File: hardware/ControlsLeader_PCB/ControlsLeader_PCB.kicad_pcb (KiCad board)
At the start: 2 copper layers, 72.5 x 61.5 mm, 3 parts, among them J1 CarCANConnector, J2 PeripheralCAN, U1 LeaderSOM

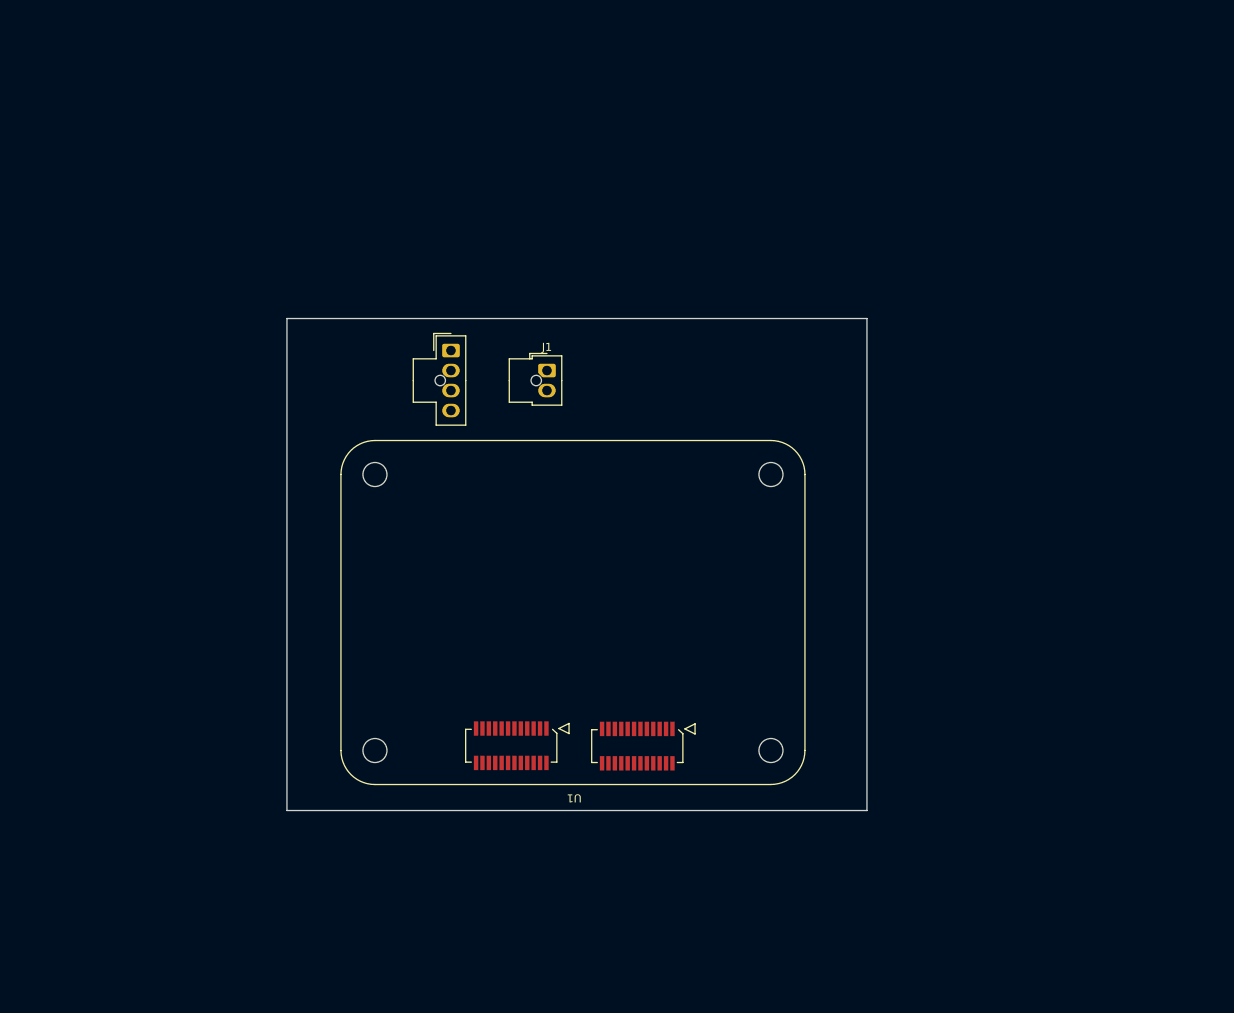
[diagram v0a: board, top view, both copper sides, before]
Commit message: Schematic Ready for Review - Just need FET footprints to be confirmed
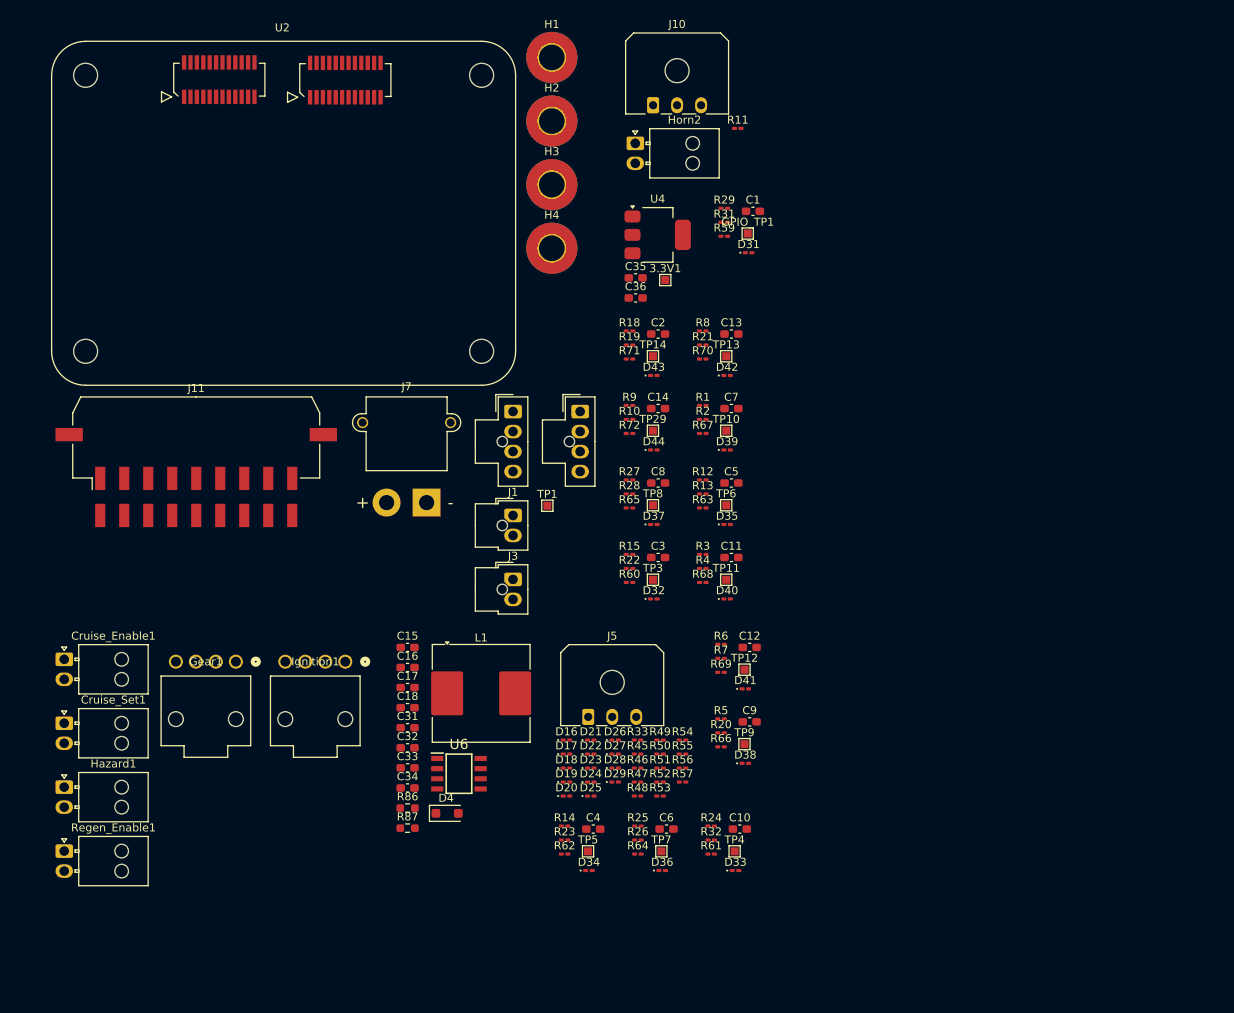
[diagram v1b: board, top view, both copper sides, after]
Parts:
- removed U1: LeaderSOM, UTSVT_Special:LeaderSOM
- added 3.3V1: TestPoint, TestPoint:TestPoint_Pad_1.0x1.0mm, F.Cu at (157.8, 68.2)
- added C1: 5uF, Capacitor_SMD:C_0603_1608Metric_Pad1.08x0.95mm_HandSolder, F.Cu at (168.7, 59.6)
- added C10: 5uF, Capacitor_SMD:C_0603_1608Metric_Pad1.08x0.95mm_HandSolder, F.Cu at (167.1, 136.8)
- added C11: 5uF, Capacitor_SMD:C_0603_1608Metric_Pad1.08x0.95mm_HandSolder, F.Cu at (166.1, 102.9)
- added C12: 5uF, Capacitor_SMD:C_0603_1608Metric_Pad1.08x0.95mm_HandSolder, F.Cu at (168.3, 114.1)
- added C13: 5uF, Capacitor_SMD:C_0603_1608Metric_Pad1.08x0.95mm_HandSolder, F.Cu at (166.1, 74.9)
- added C14: 5uF, Capacitor_SMD:C_0603_1608Metric_Pad1.08x0.95mm_HandSolder, F.Cu at (156.9, 84.2)
- added C15: 10uF, Capacitor_SMD:C_0603_1608Metric_Pad1.08x0.95mm_HandSolder, F.Cu at (125.6, 114.1)
- added C16: 1uF, Capacitor_SMD:C_0603_1608Metric_Pad1.08x0.95mm_HandSolder, F.Cu at (125.6, 116.6)
- added C17: 10nF, Capacitor_SMD:C_0603_1608Metric_Pad1.08x0.95mm_HandSolder, F.Cu at (125.6, 119.1)
- added C18: 3.3nF, Capacitor_SMD:C_0603_1608Metric_Pad1.08x0.95mm_HandSolder, F.Cu at (125.6, 121.6)
- added C2: 5uF, Capacitor_SMD:C_0603_1608Metric_Pad1.08x0.95mm_HandSolder, F.Cu at (156.9, 74.9)
- added C3: 5uF, Capacitor_SMD:C_0603_1608Metric_Pad1.08x0.95mm_HandSolder, F.Cu at (156.9, 102.9)
- added C31: 0.1uF, Capacitor_SMD:C_0603_1608Metric_Pad1.08x0.95mm_HandSolder, F.Cu at (125.6, 124.2)
- added C32: 10uF, Capacitor_SMD:C_0603_1608Metric_Pad1.08x0.95mm_HandSolder, F.Cu at (125.6, 126.7)
- added C33: 10uF, Capacitor_SMD:C_0603_1608Metric_Pad1.08x0.95mm_HandSolder, F.Cu at (125.6, 129.2)
- added C34: 10uF, Capacitor_SMD:C_0603_1608Metric_Pad1.08x0.95mm_HandSolder, F.Cu at (125.6, 131.7)
- added C35: 10uF, Capacitor_SMD:C_0603_1608Metric_Pad1.08x0.95mm_HandSolder, F.Cu at (154.1, 67.9)
- added C36: 10uF, Capacitor_SMD:C_0603_1608Metric_Pad1.08x0.95mm_HandSolder, F.Cu at (154.1, 70.4)
- added C4: 5uF, Capacitor_SMD:C_0603_1608Metric_Pad1.08x0.95mm_HandSolder, F.Cu at (148.8, 136.8)
- added C5: 5uF, Capacitor_SMD:C_0603_1608Metric_Pad1.08x0.95mm_HandSolder, F.Cu at (166.1, 93.6)
- added C6: 5uF, Capacitor_SMD:C_0603_1608Metric_Pad1.08x0.95mm_HandSolder, F.Cu at (157.9, 136.8)
- added C7: 5uF, Capacitor_SMD:C_0603_1608Metric_Pad1.08x0.95mm_HandSolder, F.Cu at (166.1, 84.2)
- added C8: 5uF, Capacitor_SMD:C_0603_1608Metric_Pad1.08x0.95mm_HandSolder, F.Cu at (156.9, 93.6)
- added C9: 5uF, Capacitor_SMD:C_0603_1608Metric_Pad1.08x0.95mm_HandSolder, F.Cu at (168.3, 123.4)
- added Cruise_Enable1: SW_Push, Connector_Molex:Molex_Nano-Fit_105313-xx02_1x02_P2.50mm_Horizontal, F.Cu at (82.7, 115.6)
- added Cruise_Set1: SW_Push, Connector_Molex:Molex_Nano-Fit_105313-xx02_1x02_P2.50mm_Horizontal, F.Cu at (82.7, 123.6)
- added D16: 0603_SMD, LED_SMD:LED_0201_0603Metric_Pad0.64x0.40mm_HandSolder, F.Cu at (145.4, 125.7)
- added D17: 0603_SMD, LED_SMD:LED_0201_0603Metric_Pad0.64x0.40mm_HandSolder, F.Cu at (145.4, 127.4)
- added D18: 0603_SMD, LED_SMD:LED_0201_0603Metric_Pad0.64x0.40mm_HandSolder, F.Cu at (145.4, 129.2)
- added D19: 0603_SMD, LED_SMD:LED_0201_0603Metric_Pad0.64x0.40mm_HandSolder, F.Cu at (145.4, 130.9)
- added D20: 0603_SMD, LED_SMD:LED_0201_0603Metric_Pad0.64x0.40mm_HandSolder, F.Cu at (145.4, 132.7)
- added D21: 0603_SMD, LED_SMD:LED_0201_0603Metric_Pad0.64x0.40mm_HandSolder, F.Cu at (148.5, 125.7)
- added D22: 0603_SMD, LED_SMD:LED_0201_0603Metric_Pad0.64x0.40mm_HandSolder, F.Cu at (148.5, 127.4)
- added D23: 0603_SMD, LED_SMD:LED_0201_0603Metric_Pad0.64x0.40mm_HandSolder, F.Cu at (148.5, 129.2)
- added D24: 0603_SMD, LED_SMD:LED_0201_0603Metric_Pad0.64x0.40mm_HandSolder, F.Cu at (148.5, 130.9)
- added D25: 0603_SMD, LED_SMD:LED_0201_0603Metric_Pad0.64x0.40mm_HandSolder, F.Cu at (148.5, 132.7)
- added D26: 0603_SMD, LED_SMD:LED_0201_0603Metric_Pad0.64x0.40mm_HandSolder, F.Cu at (151.5, 125.7)
- added D27: 0603_SMD, LED_SMD:LED_0201_0603Metric_Pad0.64x0.40mm_HandSolder, F.Cu at (151.5, 127.4)
- added D28: 0603_SMD, LED_SMD:LED_0201_0603Metric_Pad0.64x0.40mm_HandSolder, F.Cu at (151.5, 129.2)
- added D29: 0603_SMD, LED_SMD:LED_0201_0603Metric_Pad0.64x0.40mm_HandSolder, F.Cu at (151.5, 130.9)
- added D31: GPIO_Status_Blue, LED_SMD:LED_0201_0603Metric_Pad0.64x0.40mm_HandSolder, F.Cu at (168.2, 64.8)
- added D32: GPIO_Status_Blue, LED_SMD:LED_0201_0603Metric_Pad0.64x0.40mm_HandSolder, F.Cu at (156.4, 108.0)
- added D33: GPIO_Status_Blue, LED_SMD:LED_0201_0603Metric_Pad0.64x0.40mm_HandSolder, F.Cu at (166.6, 142.0)
- added D34: GPIO_Status_Blue, LED_SMD:LED_0201_0603Metric_Pad0.64x0.40mm_HandSolder, F.Cu at (148.2, 142.0)
- added D35: GPIO_Status_Blue, LED_SMD:LED_0201_0603Metric_Pad0.64x0.40mm_HandSolder, F.Cu at (165.5, 98.7)
- added D36: GPIO_Status_Blue, LED_SMD:LED_0201_0603Metric_Pad0.64x0.40mm_HandSolder, F.Cu at (157.4, 142.0)
- added D37: GPIO_Status_Blue, LED_SMD:LED_0201_0603Metric_Pad0.64x0.40mm_HandSolder, F.Cu at (156.4, 98.7)
- added D38: GPIO_Status_Blue, LED_SMD:LED_0201_0603Metric_Pad0.64x0.40mm_HandSolder, F.Cu at (167.8, 128.6)
- added D39: GPIO_Status_Blue, LED_SMD:LED_0201_0603Metric_Pad0.64x0.40mm_HandSolder, F.Cu at (165.5, 89.4)
- added D4: MBR230S1F, Diode_SMD:D_SOD-123F, F.Cu at (130.5, 134.8)
- added D40: GPIO_Status_Blue, LED_SMD:LED_0201_0603Metric_Pad0.64x0.40mm_HandSolder, F.Cu at (165.5, 108.0)
- added D41: GPIO_Status_Blue, LED_SMD:LED_0201_0603Metric_Pad0.64x0.40mm_HandSolder, F.Cu at (167.8, 119.3)
- added D42: GPIO_Status_Blue, LED_SMD:LED_0201_0603Metric_Pad0.64x0.40mm_HandSolder, F.Cu at (165.5, 80.1)
- added D43: GPIO_Status_Blue, LED_SMD:LED_0201_0603Metric_Pad0.64x0.40mm_HandSolder, F.Cu at (156.4, 80.1)
- added D44: GPIO_Status_Blue, LED_SMD:LED_0201_0603Metric_Pad0.64x0.40mm_HandSolder, F.Cu at (156.4, 89.4)
- added GPIO_TP1: TestPoint, TestPoint:TestPoint_Pad_1.0x1.0mm, F.Cu at (168.1, 62.4)
- added Gear1: SW_SP3T, nanofits_1x04:CONN_SD-105313-100_04_MOL, F.Cu at (104.1, 115.9)
- added H1: M.3, MountingHole:MountingHole_3.2mm_M3_Pad_TopBottom, F.Cu at (143.6, 40.4)
- added H2: M.3, MountingHole:MountingHole_3.2mm_M3_Pad_TopBottom, F.Cu at (143.6, 48.3)
- added H3: M.3, MountingHole:MountingHole_3.2mm_M3_Pad_TopBottom, F.Cu at (143.6, 56.3)
- added H4: M.3, MountingHole:MountingHole_3.2mm_M3_Pad_TopBottom, F.Cu at (143.6, 64.2)
- added Hazard1: SW_Push, Connector_Molex:Molex_Nano-Fit_105313-xx02_1x02_P2.50mm_Horizontal, F.Cu at (82.7, 131.6)
- added Horn2: SW_Push, Connector_Molex:Molex_Nano-Fit_105313-xx02_1x02_P2.50mm_Horizontal, F.Cu at (154.0, 51.1)
- added Ignition1: SW_SP3T, nanofits_1x04:CONN_SD-105313-100_04_MOL, F.Cu at (117.8, 115.9)
- added J10: Indicator_Switch, Connector_Molex:Molex_Micro-Fit_3.0_43650-0300_1x03_P3.00mm_Horizontal, F.Cu at (156.3, 46.3)
- added J11: Nanofit_2Rows-19Pins, Connector_Molex:Molex_Micro-Fit_3.0_43045-1810_2x09-1MP_P3.00mm_Horizontal, F.Cu at (99.2, 95.3)
- added J3: CarCANConnector_In, UTSVT_Connectors:Molex_Nano-Fit_105309-xx02_1x02_P2.50mm_Vertical, F.Cu at (138.8, 105.6)
- added J4: PeripheralCAN_in, UTSVT_Connectors:Molex_Nano-Fit_105309-xx04_1x04_P2.50mm_Vertical, F.Cu at (146.9, 87.7)
- added J5: BPS_Fault_LED, Connector_Molex:Molex_Micro-Fit_3.0_43650-0300_1x03_P3.00mm_Horizontal, F.Cu at (148.2, 122.8)
- added J7: Dash_LSOM_PWR, UTSVT_Connectors:AMASS_XT30PW-M_1x02_P2.50mm_Horizontal, F.Cu at (128.0, 96.0)
- added L1: 100uH, Inductor_SMD:L_Coilcraft_MSS1246-XXX, F.Cu at (134.8, 119.9)
- added R1: 10k, Capacitor_SMD:C_0201_0603Metric_Pad0.64x0.40mm_HandSolder, F.Cu at (162.5, 83.9)
- added R10: 100k, Capacitor_SMD:C_0201_0603Metric_Pad0.64x0.40mm_HandSolder, F.Cu at (153.3, 85.6)
- added R11: 10k, Capacitor_SMD:C_0201_0603Metric_Pad0.64x0.40mm_HandSolder, F.Cu at (166.8, 49.2)
- added R12: 10k, Capacitor_SMD:C_0201_0603Metric_Pad0.64x0.40mm_HandSolder, F.Cu at (162.5, 93.2)
- added R13: 100k, Capacitor_SMD:C_0201_0603Metric_Pad0.64x0.40mm_HandSolder, F.Cu at (162.5, 94.9)
- added R14: 10k, Capacitor_SMD:C_0201_0603Metric_Pad0.64x0.40mm_HandSolder, F.Cu at (145.2, 136.4)
- added R15: 10k, Capacitor_SMD:C_0201_0603Metric_Pad0.64x0.40mm_HandSolder, F.Cu at (153.3, 102.5)
- added R18: 10k, Capacitor_SMD:C_0201_0603Metric_Pad0.64x0.40mm_HandSolder, F.Cu at (153.3, 74.6)
- added R19: 100k, Capacitor_SMD:C_0201_0603Metric_Pad0.64x0.40mm_HandSolder, F.Cu at (153.3, 76.3)
- added R2: 100k, Capacitor_SMD:C_0201_0603Metric_Pad0.64x0.40mm_HandSolder, F.Cu at (162.5, 85.6)
- added R20: 100k, Capacitor_SMD:C_0201_0603Metric_Pad0.64x0.40mm_HandSolder, F.Cu at (164.8, 124.8)
- added R21: 100k, Capacitor_SMD:C_0201_0603Metric_Pad0.64x0.40mm_HandSolder, F.Cu at (162.5, 76.3)
- added R22: 100k, Capacitor_SMD:C_0201_0603Metric_Pad0.64x0.40mm_HandSolder, F.Cu at (153.3, 104.2)
- added R23: 100k, Capacitor_SMD:C_0201_0603Metric_Pad0.64x0.40mm_HandSolder, F.Cu at (145.2, 138.2)
- added R24: 10k, Capacitor_SMD:C_0201_0603Metric_Pad0.64x0.40mm_HandSolder, F.Cu at (163.5, 136.4)
- added R25: 10k, Capacitor_SMD:C_0201_0603Metric_Pad0.64x0.40mm_HandSolder, F.Cu at (154.4, 136.4)
- added R26: 100k, Capacitor_SMD:C_0201_0603Metric_Pad0.64x0.40mm_HandSolder, F.Cu at (154.4, 138.2)
- added R27: 10k, Capacitor_SMD:C_0201_0603Metric_Pad0.64x0.40mm_HandSolder, F.Cu at (153.3, 93.2)
- added R28: 100k, Capacitor_SMD:C_0201_0603Metric_Pad0.64x0.40mm_HandSolder, F.Cu at (153.3, 94.9)
- added R29: 10k, Capacitor_SMD:C_0201_0603Metric_Pad0.64x0.40mm_HandSolder, F.Cu at (165.2, 59.2)
- added R3: 10k, Capacitor_SMD:C_0201_0603Metric_Pad0.64x0.40mm_HandSolder, F.Cu at (162.5, 102.5)
- added R31: 100k, Capacitor_SMD:C_0201_0603Metric_Pad0.64x0.40mm_HandSolder, F.Cu at (165.2, 61.0)
- added R32: 100k, Capacitor_SMD:C_0201_0603Metric_Pad0.64x0.40mm_HandSolder, F.Cu at (163.5, 138.2)
- added R33: 65, Capacitor_SMD:C_0201_0603Metric_Pad0.64x0.40mm_HandSolder, F.Cu at (154.3, 125.7)
- added R4: 100k, Capacitor_SMD:C_0201_0603Metric_Pad0.64x0.40mm_HandSolder, F.Cu at (162.5, 104.2)
- added R45: 65, Capacitor_SMD:C_0201_0603Metric_Pad0.64x0.40mm_HandSolder, F.Cu at (154.3, 127.4)
- added R46: 65, Capacitor_SMD:C_0201_0603Metric_Pad0.64x0.40mm_HandSolder, F.Cu at (154.3, 129.2)
- added R47: 1.1k, Capacitor_SMD:C_0201_0603Metric_Pad0.64x0.40mm_HandSolder, F.Cu at (154.3, 130.9)
- added R48: 20, Capacitor_SMD:C_0201_0603Metric_Pad0.64x0.40mm_HandSolder, F.Cu at (154.3, 132.7)
- added R49: 20, Capacitor_SMD:C_0201_0603Metric_Pad0.64x0.40mm_HandSolder, F.Cu at (157.1, 125.7)
- added R5: 10k, Capacitor_SMD:C_0201_0603Metric_Pad0.64x0.40mm_HandSolder, F.Cu at (164.8, 123.0)
- added R50: 20, Capacitor_SMD:C_0201_0603Metric_Pad0.64x0.40mm_HandSolder, F.Cu at (157.1, 127.4)
- added R51: 20, Capacitor_SMD:C_0201_0603Metric_Pad0.64x0.40mm_HandSolder, F.Cu at (157.1, 129.2)
- added R52: 20, Capacitor_SMD:C_0201_0603Metric_Pad0.64x0.40mm_HandSolder, F.Cu at (157.1, 130.9)
- added R53: 20, Capacitor_SMD:C_0201_0603Metric_Pad0.64x0.40mm_HandSolder, F.Cu at (157.1, 132.7)
- added R54: 20, Capacitor_SMD:C_0201_0603Metric_Pad0.64x0.40mm_HandSolder, F.Cu at (159.9, 125.7)
- added R55: 65, Capacitor_SMD:C_0201_0603Metric_Pad0.64x0.40mm_HandSolder, F.Cu at (159.9, 127.4)
- added R56: 65, Capacitor_SMD:C_0201_0603Metric_Pad0.64x0.40mm_HandSolder, F.Cu at (159.9, 129.2)
- added R57: 65, Capacitor_SMD:C_0201_0603Metric_Pad0.64x0.40mm_HandSolder, F.Cu at (159.9, 130.9)
- added R59: 150, Capacitor_SMD:C_0201_0603Metric_Pad0.64x0.40mm_HandSolder, F.Cu at (165.2, 62.7)
- added R6: 10k, Capacitor_SMD:C_0201_0603Metric_Pad0.64x0.40mm_HandSolder, F.Cu at (164.8, 113.7)
- added R60: 150, Capacitor_SMD:C_0201_0603Metric_Pad0.64x0.40mm_HandSolder, F.Cu at (153.3, 106.0)
- added R61: 150, Capacitor_SMD:C_0201_0603Metric_Pad0.64x0.40mm_HandSolder, F.Cu at (163.5, 139.9)
- added R62: 150, Capacitor_SMD:C_0201_0603Metric_Pad0.64x0.40mm_HandSolder, F.Cu at (145.2, 139.9)
- added R63: 150, Capacitor_SMD:C_0201_0603Metric_Pad0.64x0.40mm_HandSolder, F.Cu at (162.5, 96.7)
- added R64: 150, Capacitor_SMD:C_0201_0603Metric_Pad0.64x0.40mm_HandSolder, F.Cu at (154.4, 139.9)
- added R65: 150, Capacitor_SMD:C_0201_0603Metric_Pad0.64x0.40mm_HandSolder, F.Cu at (153.3, 96.7)
- added R66: 150, Capacitor_SMD:C_0201_0603Metric_Pad0.64x0.40mm_HandSolder, F.Cu at (164.8, 126.5)
- added R67: 150, Capacitor_SMD:C_0201_0603Metric_Pad0.64x0.40mm_HandSolder, F.Cu at (162.5, 87.4)
- added R68: 150, Capacitor_SMD:C_0201_0603Metric_Pad0.64x0.40mm_HandSolder, F.Cu at (162.5, 106.0)
- added R69: 150, Capacitor_SMD:C_0201_0603Metric_Pad0.64x0.40mm_HandSolder, F.Cu at (164.8, 117.2)
- added R7: 100k, Capacitor_SMD:C_0201_0603Metric_Pad0.64x0.40mm_HandSolder, F.Cu at (164.8, 115.5)
- added R70: 150, Capacitor_SMD:C_0201_0603Metric_Pad0.64x0.40mm_HandSolder, F.Cu at (162.5, 78.1)
- added R71: 150, Capacitor_SMD:C_0201_0603Metric_Pad0.64x0.40mm_HandSolder, F.Cu at (153.3, 78.1)
- added R72: 150, Capacitor_SMD:C_0201_0603Metric_Pad0.64x0.40mm_HandSolder, F.Cu at (153.3, 87.4)
- added R8: 10k, Capacitor_SMD:C_0201_0603Metric_Pad0.64x0.40mm_HandSolder, F.Cu at (162.5, 74.6)
- added R86: 16k, Resistor_SMD:R_0603_1608Metric_Pad0.98x0.95mm_HandSolder, F.Cu at (125.6, 134.2)
- added R87: ROSC, Resistor_SMD:R_0603_1608Metric_Pad0.98x0.95mm_HandSolder, F.Cu at (125.6, 136.7)
- added R9: 10k, Capacitor_SMD:C_0201_0603Metric_Pad0.64x0.40mm_HandSolder, F.Cu at (153.3, 83.9)
- added Regen_Enable1: SW_Push, Connector_Molex:Molex_Nano-Fit_105313-xx02_1x02_P2.50mm_Horizontal, F.Cu at (82.7, 139.6)
- added TP1: TestPoint, TestPoint:TestPoint_Pad_1.0x1.0mm, F.Cu at (143.0, 96.4)
- added TP10: TestPoint, TestPoint:TestPoint_Pad_1.0x1.0mm, F.Cu at (165.4, 87.0)
- added TP11: TestPoint, TestPoint:TestPoint_Pad_1.0x1.0mm, F.Cu at (165.4, 105.7)
- added TP12: TestPoint, TestPoint:TestPoint_Pad_1.0x1.0mm, F.Cu at (167.7, 116.9)
- added TP13: TestPoint, TestPoint:TestPoint_Pad_1.0x1.0mm, F.Cu at (165.4, 77.7)
- added TP14: TestPoint, TestPoint:TestPoint_Pad_1.0x1.0mm, F.Cu at (156.2, 77.7)
- added TP29: TestPoint, TestPoint:TestPoint_Pad_1.0x1.0mm, F.Cu at (156.2, 87.0)
- added TP3: TestPoint, TestPoint:TestPoint_Pad_1.0x1.0mm, F.Cu at (156.2, 105.7)
- added TP4: TestPoint, TestPoint:TestPoint_Pad_1.0x1.0mm, F.Cu at (166.5, 139.6)
- added TP5: TestPoint, TestPoint:TestPoint_Pad_1.0x1.0mm, F.Cu at (148.1, 139.6)
- added TP6: TestPoint, TestPoint:TestPoint_Pad_1.0x1.0mm, F.Cu at (165.4, 96.3)
- added TP7: TestPoint, TestPoint:TestPoint_Pad_1.0x1.0mm, F.Cu at (157.3, 139.6)
- added TP8: TestPoint, TestPoint:TestPoint_Pad_1.0x1.0mm, F.Cu at (156.2, 96.3)
- added TP9: TestPoint, TestPoint:TestPoint_Pad_1.0x1.0mm, F.Cu at (167.7, 126.2)
- added U2: LeaderSOM, UTSVT_Special:LeaderSOM, F.Cu at (109.9, 37.1)
- added U4: LT1963AEST-3.3#TRPBF, Package_TO_SOT_SMD:SOT-223-3_TabPin2, F.Cu at (156.8, 62.5)
- added U6: TPS5405DR, UTSVT_Power:TPS5405DR, F.Cu at (132.0, 129.9)
- J1: value CarCANConnector -> CarCANConnector_Out
- J2: value PeripheralCAN -> PeripheralCAN_out
- moved J1 18.6 mm to (138.8, 97.6)
- moved J2 10.9 mm to (138.5, 87.7)
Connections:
- J1 pad 1: unconnected-(J1-CAN_H-Pad1) -> /CarCan_H
- J1 pad 2: unconnected-(J1-CAN_L-Pad2) -> /CarCan_L
- J2 pad 1: unconnected-(J2-24V-Pad1) -> +24V
- J2 pad 3: unconnected-(J2-CAN_H-Pad3) -> /PerCan_H
- J2 pad 4: unconnected-(J2-CAN_L-Pad4) -> /PerCan_L
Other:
- board outline removed

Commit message: Schematic RevA
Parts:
- removed C1, C10, C11, C12, C14, C2, C3, C4, C5, C6, C7, C8, C9: 5uF, Capacitor_SMD:C_0603_1608Metric_Pad1.08x0.95mm_HandSolder
- removed Cruise_Enable1, Cruise_Set1, Hazard1, Horn2, Regen_Enable1: SW_Push, Connector_Molex:Molex_Nano-Fit_105313-xx02_1x02_P2.50mm_Horizontal
- removed D16, D17, D18, D19, D20, D21, D22, D23, D24, D25, D26, D27, D28, D29: 0603_SMD, LED_SMD:LED_0201_0603Metric_Pad0.64x0.40mm_HandSolder
- removed D31, D32, D33, D34, D35, D36, D37, D38, D39, D40, D41, D42, D43, D44: GPIO_Status_Blue, LED_SMD:LED_0201_0603Metric_Pad0.64x0.40mm_HandSolder
- removed GPIO_TP1, TP1, TP10, TP11, TP12, TP14, TP29, TP3, TP4, TP5, TP6, TP7, TP8, TP9: TestPoint, TestPoint:TestPoint_Pad_1.0x1.0mm
- removed Gear1, Ignition1: SW_SP3T, nanofits_1x04:CONN_SD-105313-100_04_MOL
- removed J10: Indicator_Switch, Connector_Molex:Molex_Micro-Fit_3.0_43650-0300_1x03_P3.00mm_Horizontal
- removed J11: Nanofit_2Rows-19Pins, Connector_Molex:Molex_Micro-Fit_3.0_43045-1810_2x09-1MP_P3.00mm_Horizontal
- removed J5: BPS_Fault_LED, Connector_Molex:Molex_Micro-Fit_3.0_43650-0300_1x03_P3.00mm_Horizontal
- removed R1, R12, R14, R15, R18, R24, R25, R27, R29, R3, R5, R6, R9: 10k, Capacitor_SMD:C_0201_0603Metric_Pad0.64x0.40mm_HandSolder
- removed R10, R13, R19, R2, R20, R22, R23, R26, R28, R31, R32, R4, R7: 100k, Capacitor_SMD:C_0201_0603Metric_Pad0.64x0.40mm_HandSolder
- removed R33, R45, R46, R55, R56, R57: 65, Capacitor_SMD:C_0201_0603Metric_Pad0.64x0.40mm_HandSolder
- removed R47: 1.1k, Capacitor_SMD:C_0201_0603Metric_Pad0.64x0.40mm_HandSolder
- removed R48, R49, R50, R51, R52, R53, R54: 20, Capacitor_SMD:C_0201_0603Metric_Pad0.64x0.40mm_HandSolder
- removed R59, R60, R61, R62, R63, R64, R65, R66, R67, R68, R69, R70, R71, R72: 150, Capacitor_SMD:C_0201_0603Metric_Pad0.64x0.40mm_HandSolder
- added F1: Fuse, Fuse:Fuseholder_Blade_Mini_Keystone_3568, F.Cu at (145.2, 89.9)
- added F2: Fuse, Fuse:Fuseholder_Blade_Mini_Keystone_3568, F.Cu at (198.1, 132.0)
- added J15: IgnConn_01x04, Connector_Molex:Molex_Nano-Fit_105313-xx04_1x04_P2.50mm_Horizontal, F.Cu at (214.2, 76.0)
- added J16: SteeringConn_01x05, Connector_Molex:Molex_Nano-Fit_105313-xx05_1x05_P2.50mm_Horizontal, F.Cu at (109.0, 144.3)
- added J17: Conn_01x02, Connector_Molex:Molex_Nano-Fit_105313-xx02_1x02_P2.50mm_Horizontal, F.Cu at (214.3, 132.3)
- added J6: DashConn1_2Rows-09Pins, Connector_Molex:Molex_Nano-Fit_105313-xx08_1x08_P2.50mm_Horizontal, F.Cu at (87.4, 93.7)
- added J8: DashConn2_2Rows-09Pins, Connector_Molex:Molex_Nano-Fit_105313-xx08_1x08_P2.50mm_Horizontal, F.Cu at (87.2, 128.5)
- added Q14: NMOS, LSOM_IRLM:SOT23, F.Cu at (103.0, 136.2)
- added Q6: NMOS, LSOM_IRLM:SOT23, F.Cu at (197.2, 141.8)
- added Q9: NMOS, LSOM_IRLM:SOT23, F.Cu at (103.9, 124.2)
- R11, R8: footprint Capacitor_SMD:C_0201_0603Metric_Pad0.64x0.40mm_HandSolder -> Capacitor_SMD:C_0603_1608Metric_Pad1.08x0.95mm_HandSolder
- R21: value 100k -> 150; footprint Capacitor_SMD:C_0201_0603Metric_Pad0.64x0.40mm_HandSolder -> Capacitor_SMD:C_0603_1608Metric_Pad1.08x0.95mm_HandSolder
- moved U2 124.9 mm to (147.4, 156.2), turned to 180 degrees
- moved H1 123.5 mm to (83.0, 148.0)
- moved H4 114.0 mm to (220.0, 148.8)
- moved TP13 103.9 mm to (94.0, 153.2)
- moved R11 100.7 mm to (197.2, 145.3), turned to -90 degrees
- moved J7 84.4 mm to (211.3, 109.1), turned to -90 degrees
- moved R21 76.9 mm to (114.1, 136.0), turned to 180 degrees
- moved H3 76.6 mm to (220.0, 61.8)
- moved R8 75.0 mm to (112.0, 130.1), turned to -90 degrees
- moved C13 74.7 mm to (112.0, 126.5), turned to 90 degrees
- moved D4 72.1 mm to (179.8, 82.2), turned to 90 degrees
- moved C34 67.5 mm to (185.3, 100.3), turned to -90 degrees
- moved C31 64.7 mm to (178.4, 86.8)
- moved C33 64.5 mm to (183.3, 100.3), turned to -90 degrees
- moved R86 63.6 mm to (176.3, 95.9), turned to -90 degrees
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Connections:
- net /3.3V_LDO renamed /5v_3.3v_LDO/3.3V_LDO
- C13 pad 2: /Steering_Wheel/NMOS Switch3/3.3V_LDO -> /Steering_Wheel/NMOS Switch1/3.3V_LDO_Switch
- R21 pad 1: /3.3V_LSOM -> Net-(D6-K)
- R21 pad 2: /Horn_GPIO_IN -> GND
- R8 pad 2: /Steering_Wheel/NMOS Switch3/3.3V_LDO -> /Dash/NMOS Switch6/3.3V_LDO_Switch
- TP13 pad 1: /Horn_GPIO_IN -> /Right_Blinker_ON
- U2 pad 31: /Extra_LED6 -> /Regen_Active_GPIO_IN
